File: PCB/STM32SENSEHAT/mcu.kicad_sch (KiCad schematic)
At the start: 26 parts, among them J1 USB_B_Micro, J2 Conn_01x24_Socket, J3 Conn_01x24_Socket, J5 Conn_01x24_Pin, J6 Conn_01x10_Pin, J7 Conn_01x04_Socket, J7 Conn_01x05_Pin, J8 Conn_01x24_Pin, J9 Conn_01x05_Socket, SW1 SW_Push, U3 FT230XQ, U6 CAT24C256

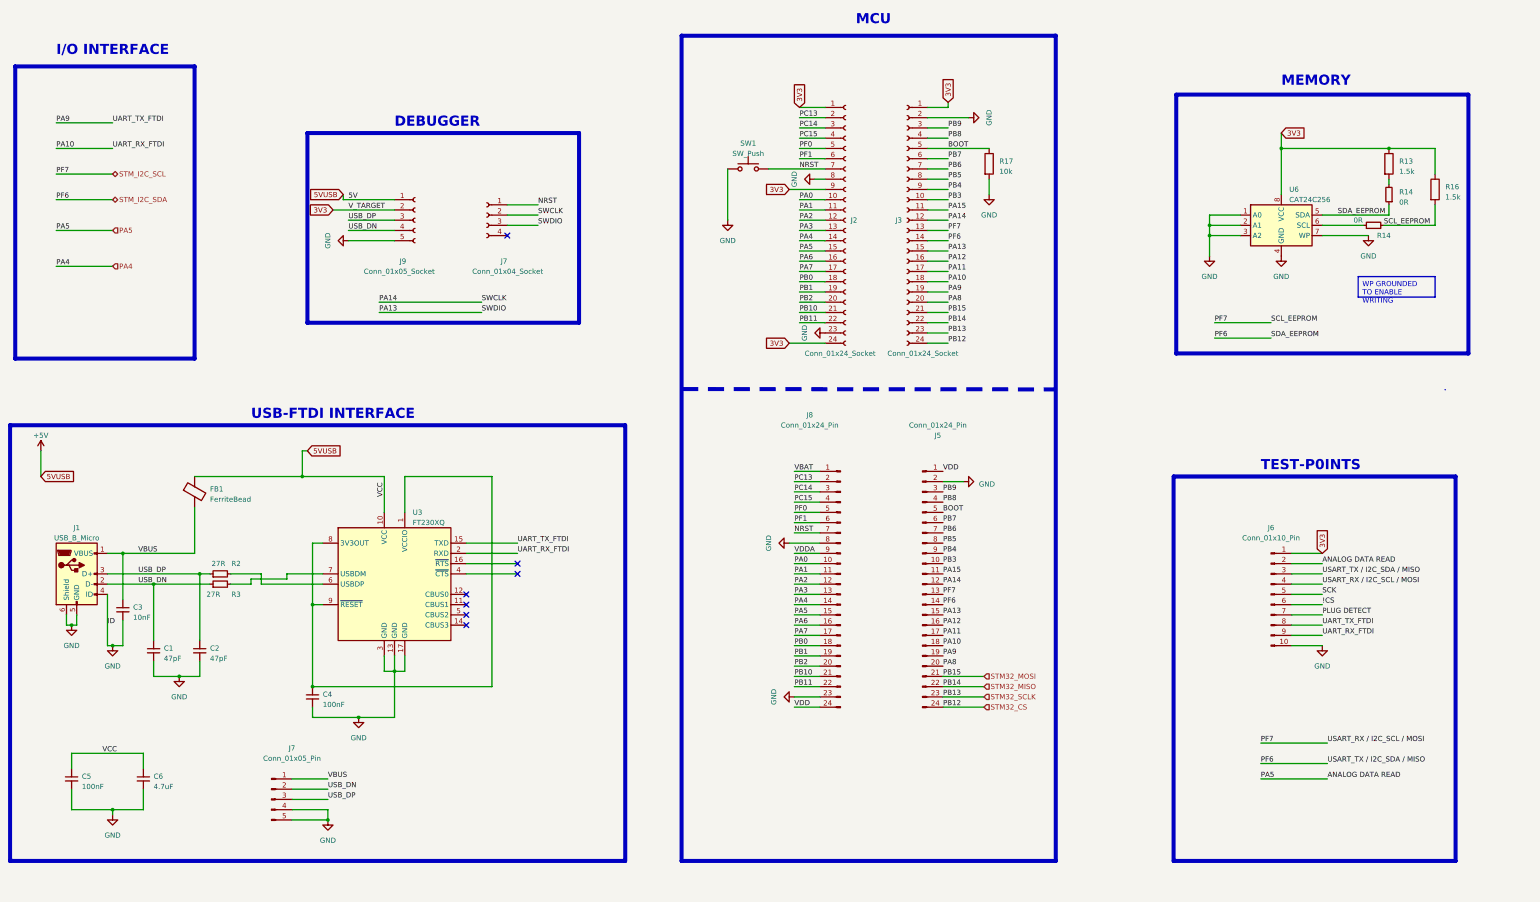
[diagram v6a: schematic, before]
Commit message: Rework of Power,MCU and Sensor Schematic
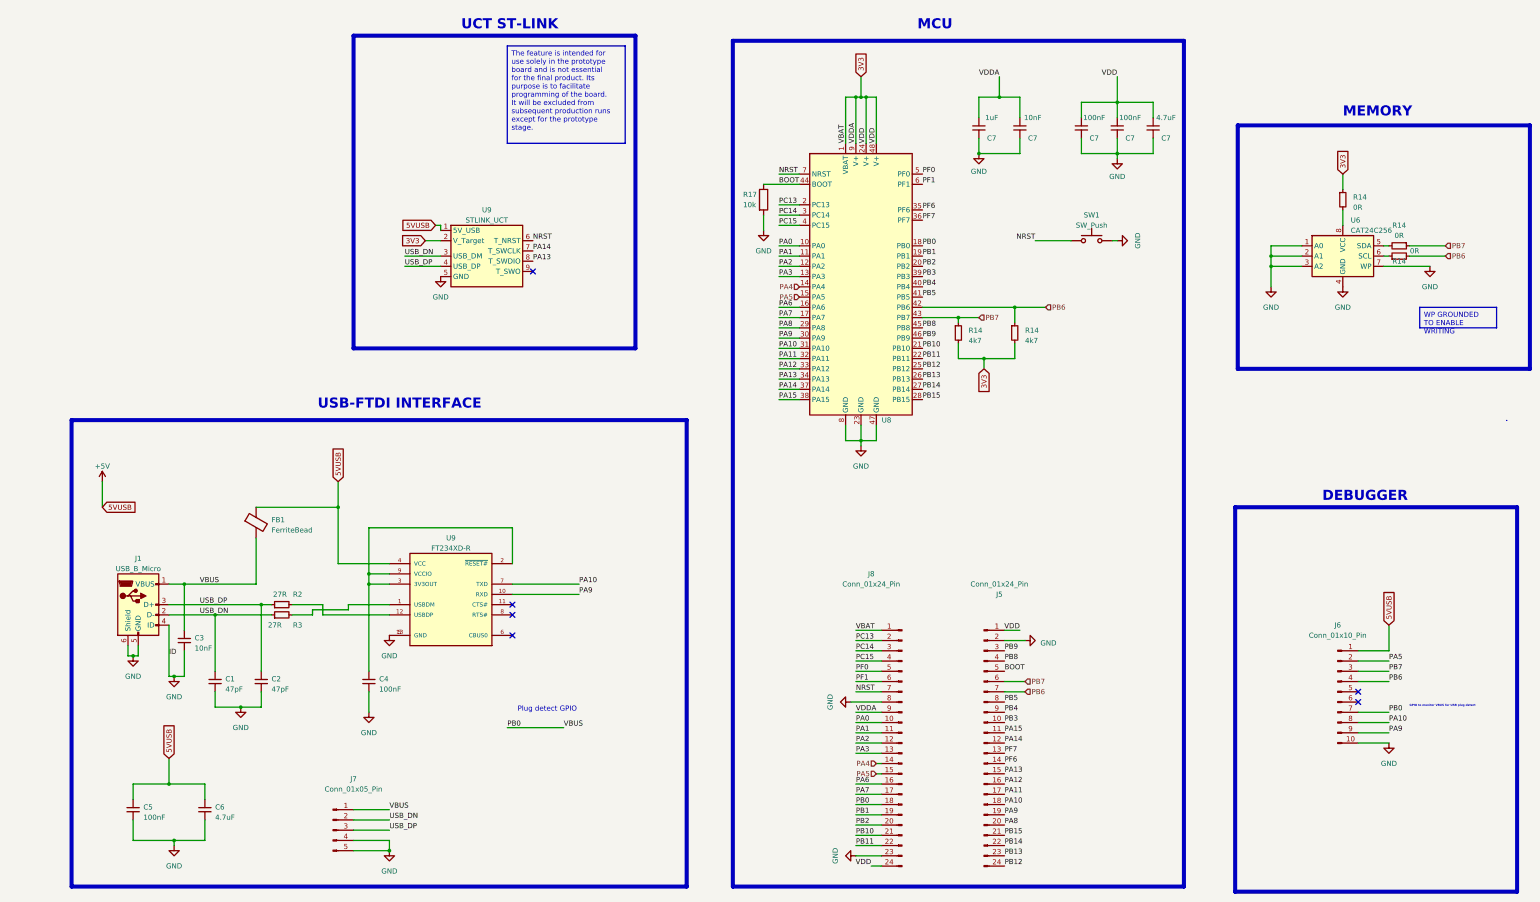
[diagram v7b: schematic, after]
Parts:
- removed J2, J3: Conn_01x24_Socket, Connector_PinSocket_2.54mm:PinSocket_1x24_P2.54mm_Vertical, symbol Connector:Conn_01x24_Socket
- removed J7: Conn_01x04_Socket, Connector_PinSocket_2.54mm:PinSocket_1x04_P2.54mm_Vertical, symbol Connector:Conn_01x04_Socket
- removed J9: Conn_01x05_Socket, Connector_PinSocket_2.54mm:PinSocket_1x05_P2.54mm_Vertical, symbol Connector:Conn_01x05_Socket
- removed R13, R16: 1.5k, Resistor_SMD:R_0805_2012Metric, symbol Device:R
- removed R14 (x2): 0R, Resistor_SMD:R_0805_2012Metric, symbol Device:R_Small
- removed U3: FT230XQ, Package_DFN_QFN:QFN-16-1EP_4x4mm_P0.65mm_EP2.1x2.1mm, symbol Interface_USB:FT230XQ
- added C7 (x2): 100nF, JLCfootprint:C0805, symbol Device:C_Small
- added C7: 1uF, JLCfootprint:C0805, symbol Device:C_Small
- added C7: 4.7uF, JLCfootprint:C0805, symbol Device:C_Small
- added C7: 10nF, JLCfootprint:C0805, symbol Device:C_Small
- added R14 (x2): 4k7, JLCfootprint:R0805, symbol Device:R_Small
- added R14 (x3): 0R, JLCfootprint:R0805, symbol Device:R_Small
- added U8: ~, footprints:STM32F051C6T6, symbol UCT:STM32F051C6TG6_Target
- added U9: FT234XD-R, JLCfootprint:DFN-12_L3.0-W3.0-P0.45-BL-EP, symbol FT234XD-R:FT234XD-R
- added U9: STLINK_UCT, footprints:STLINK_UCT, symbol UCT:STLINK_UCT
- C1, C2, C3, C4, C5, C6: footprint Capacitor_SMD:C_0805_2012Metric -> JLCfootprint:C0805
- FB1: footprint Resistor_SMD:R_0603_1608Metric -> JLCfootprint:L0603
- J1: footprint Connector_USB:USB_Micro-AB_Molex_47590-0001 -> footprints:USB_Conn_JLC_LCSC_C404969
- R17: footprint Resistor_SMD:R_0805_2012Metric -> JLCfootprint:R0805
- R2, R3: footprint Resistor_SMD:R_0603_1608Metric -> JLCfootprint:R0603
- U6: footprint Package_SO:SOIC-8-1EP_3.9x4.9mm_P1.27mm_EP2.41x3.3mm -> JLCfootprint:SOIC-8_L4.9-W3.9-P1.27-LS6.0-BL
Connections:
- net PLUG DETECT is gone; now on net PB0: J6.7 (Pin_7)
- net VBAT is gone; now on net 3V3: J8.1 (Pin_1)
- net VBUS is gone; now on net PB0: C3.1, FB1.2, J1.1 (VBUS), J7.1 (Pin_1)
- net VDD is gone; now on net 3V3: J5.1 (Pin_1), J8.24 (Pin_24)
- net VDDA is gone; now on net 3V3: J8.9 (Pin_9)
- net +5V: now also J6.1 (Pin_1), U9.1 (5V_USB), U9.4 (VCC)
- net 3V3: now also C7.1, C7.1, C7.1, C7.1, C7.1, R14.1, R14.2, R14.2, U8.1 (VBAT), U8.24 (V+), U8.48 (V+), U8.9 (V+), U9.2 (V_Target); no longer J6.1 (Pin_1), U6.8 (VCC)
- net BOOT: now also U8.44 (BOOT)
- net GND: now also C7.2, C7.2, C7.2, C7.2, C7.2, U8.23 (GND), U8.47 (GND), U8.8 (GND), U9.13 (GND), U9.5 (GND), U9.5 (GND)
- net NRST: now also U8.7 (NRST), U9.6 (T_NRST)
- net PA0: now also U8.10 (PA0)
- net PA1: now also U8.11 (PA1)
- net PA10: now also J6.8 (Pin_8), U8.31 (PA10), U9.7 (TXD); no longer J6.9 (Pin_9)
- net PA11: now also U8.32 (PA11)
- net PA12: now also U8.33 (PA12)
- net PA13: now also U8.34 (PA13), U9.8 (T_SWDIO)
- net PA14: now also U8.37 (PA14), U9.7 (T_SWCLK)
- net PA15: now also U8.38 (PA15)
- net PA2: now also U8.12 (PA2)
- net PA3: now also U8.13 (PA3)
- net PA4: now also U8.14 (PA4)
- net PA5: now also U8.15 (PA5)
- net PA6: now also U8.16 (PA6)
- net PA7: now also U8.17 (PA7)
- net PA8: now also U8.29 (PA8)
- net PA9: now also J6.9 (Pin_9), U8.30 (PA9), U9.10 (RXD); no longer J6.8 (Pin_8)
- net PB0: now also U8.18 (PB0)
- net PB1: now also U8.19 (PB1)
- net PB10: now also U8.21 (PB10)
- net PB11: now also U8.22 (PB11)
- net PB2: now also U8.20 (PB2)
- net PB3: now also U8.39 (PB3)
- net PB4: now also U8.40 (PB4)
- net PB5: now also U8.41 (PB5)
- net PB6: now also J6.4 (Pin_4), R14.1, R14.2, U8.42 (PB6)
- net PB7: now also J6.3 (Pin_3), R14.1, R14.1, U8.43 (PB7)
- net PB8: now also U8.45 (PB8)
- net PB9: now also U8.46 (PB9)
- net PC13: now also U8.2 (PC13)
- net PC14: now also U8.3 (PC14)
- net PC15: now also U8.4 (PC15)
- net PF0: now also U8.5 (PF0)
- net PF1: now also U8.6 (PF1)
- net USB_DN: now also U9.3 (USB_DM)
- net USB_DP: now also U9.4 (USB_DP)
- net at C4.1: now also U9.2 (~{RESET#}), U9.3 (3V3OUT), U9.9 (VCCIO)
- net at R3.2: now also U9.1 (USBDM)
- net at U6.6 (SCL): now also R14.1
- net at R2.2: now also U9.12 (USBDP)
- net !CS: no longer names the net of J6.6 (Pin_6)
- net SCK: no longer names the net of J6.5 (Pin_5)
- net STM32_CS renamed PB12
- net PB12: now also U8.25 (PB12)
- net STM32_MISO renamed PB14
- net PB14: now also U8.27 (PB14)
- net STM32_MOSI renamed PB15
- net PB15: now also U8.28 (PB15)
- net STM32_SCLK renamed PB13
- net PB13: now also U8.26 (PB13)
- net STM_I2C_SCL renamed PF7
- net PF7: now also U8.36 (PF7); no longer J6.4 (Pin_4)
- removed net STM_I2C_SDA: J5.14 (Pin_14), J6.3 (Pin_3), U6.5 (SDA)
- new net: R14.2, U6.5 (SDA)
- new net: R14.2, U6.8 (VCC)
- new net PF6: J5.14 (Pin_14), U8.35 (PF6)
- no-connect marks 7 -> 6
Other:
- note added: "GPIO to monitor VBUS for USB plug detect"
- note added: "Plug detect GPIO"
- note added: "UCT ST-LINK"
- note removed: "I/O INTERFACE"
- note removed: "TEST-P0INTS"

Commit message: PCB draft
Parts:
- C1, C2, C3, C4, C5, C6: footprint JLCfootprint:C0805 -> Capacitor_SMD:C_0805_2012Metric
- C7: footprint JLCfootprint:C0805 -> Capacitor_THT:C_Disc_D5.0mm_W2.5mm_P5.00mm
- R14, R17: footprint JLCfootprint:R0805 -> Resistor_SMD:R_0805_2012Metric
- R2, R3: footprint JLCfootprint:R0603 -> Resistor_SMD:R_0805_2012Metric
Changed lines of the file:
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@@
       (effects (font (size 1.27 1.27)) (justify left))
     )
-    (property "Footprint" "JLCfootprint:R0805" (at 252.73 92.71 0)
+    (property "Footprint" "Resistor_SMD:R_0805_2012Metric" (at 252.73 92.71 0)
       (effects (font (size 1.27 1.27)) hide)
     )
@@
       (effects (font (size 1.27 1.27)) (justify left))
     )
-    (property "Footprint" "JLCfootprint:R0603" (at 85.09 160.02 0)
+    (property "Footprint" "Resistor_SMD:R_0805_2012Metric" (at 85.09 160.02 0)
       (effects (font (size 1.27 1.27)) hide)
     )
@@
       (effects (font (size 1.27 1.27)) (justify left))
     )
-    (property "Footprint" "JLCfootprint:C0805" (at 60.96 168.91 0)
+    (property "Footprint" "Capacitor_SMD:C_0805_2012Metric" (at 60.96 168.91 0)
       (effects (font (size 1.27 1.27)) hide)
     )
@@
       (effects (font (size 1.27 1.27)) (justify left))
     )
-    (property "Footprint" "JLCfootprint:R0805" (at 266.7 92.71 0)
+    (property "Footprint" "Resistor_SMD:R_0805_2012Metric" (at 266.7 92.71 0)
       (effects (font (size 1.27 1.27)) hide)
     )
@@
       (effects (font (size 1.27 1.27)))
     )
-    (property "Footprint" "JLCfootprint:R0805" (at 361.95 71.12 0)
+    (property "Footprint" "Resistor_SMD:R_0805_2012Metric" (at 361.95 71.12 0)
       (effects (font (size 1.27 1.27)) hide)
     )
@@
       (effects (font (size 1.27 1.27)))
     )
-    (property "Footprint" "JLCfootprint:C0805" (at 283.21 41.91 0)
+    (property "Footprint" "Capacitor_THT:C_Disc_D5.0mm_W2.5mm_P5.00mm" (at 283.21 41.91 0)
       (effects (font (size 1.27 1.27)) hide)
     )
@@
       (effects (font (size 1.27 1.27)) (justify left))
     )
-    (property "Footprint" "JLCfootprint:R0603" (at 85.09 162.56 0)
+    (property "Footprint" "Resistor_SMD:R_0805_2012Metric" (at 85.09 162.56 0)
       (effects (font (size 1.27 1.27)) hide)
     )
@@
       (effects (font (size 1.27 1.27)))
     )
-    (property "Footprint" "JLCfootprint:C0805" (at 257.81 41.91 0)
+    (property "Footprint" "Capacitor_THT:C_Disc_D5.0mm_W2.5mm_P5.00mm" (at 257.81 41.91 0)
       (effects (font (size 1.27 1.27)) hide)
     )
@@
       (effects (font (size 1.27 1.27)) (justify left))
     )
-    (property "Footprint" "JLCfootprint:C0805" (at 66.04 210.82 0)
+    (property "Footprint" "Capacitor_SMD:C_0805_2012Metric" (at 66.04 210.82 0)
       (effects (font (size 1.27 1.27)) hide)
     )
@@
       (effects (font (size 1.27 1.27)) (justify left))
     )
-    (property "Footprint" "JLCfootprint:C0805" (at 68.58 179.07 0)
+    (property "Footprint" "Capacitor_SMD:C_0805_2012Metric" (at 68.58 179.07 0)
       (effects (font (size 1.27 1.27)) hide)
     )
@@
       (effects (font (size 1.27 1.27)) (justify left))
     )
-    (property "Footprint" "JLCfootprint:C0805" (at 106.68 179.07 0)
+    (property "Footprint" "Capacitor_SMD:C_0805_2012Metric" (at 106.68 179.07 0)
       (effects (font (size 1.27 1.27)) hide)
     )
@@
       (effects (font (size 1.27 1.27)) (justify left))
     )
-    (property "Footprint" "JLCfootprint:C0805" (at 80.01 179.07 0)
+    (property "Footprint" "Capacitor_SMD:C_0805_2012Metric" (at 80.01 179.07 0)
       (effects (font (size 1.27 1.27)) hide)
     )
@@
       (effects (font (size 1.27 1.27)) (justify left))
     )
-    (property "Footprint" "JLCfootprint:C0805" (at 48.26 210.82 0)
+    (property "Footprint" "Capacitor_SMD:C_0805_2012Metric" (at 48.26 210.82 0)
       (effects (font (size 1.27 1.27)) hide)
     )
@@
       (effects (font (size 1.27 1.27)) (justify left))
     )
-    (property "Footprint" "JLCfootprint:R0805" (at 347.98 59.69 0)
+    (property "Footprint" "Resistor_SMD:R_0805_2012Metric" (at 347.98 59.69 0)
       (effects (font (size 1.27 1.27)) hide)
     )
@@
       (effects (font (size 1.27 1.27)) (justify left))
     )
-    (property "Footprint" "JLCfootprint:R0805" (at 202.692 59.69 90)
+    (property "Footprint" "Resistor_SMD:R_0805_2012Metric" (at 202.692 59.69 90)
       (effects (font (size 1.27 1.27)) hide)
     )
@@
       (effects (font (size 1.27 1.27)))
     )
-    (property "Footprint" "JLCfootprint:R0805" (at 361.95 73.66 0)
+    (property "Footprint" "Resistor_SMD:R_0805_2012Metric" (at 361.95 73.66 0)
       (effects (font (size 1.27 1.27)) hide)
     )
@@
       (effects (font (size 1.27 1.27)))
     )
-    (property "Footprint" "JLCfootprint:C0805" (at 300.99 41.91 0)
+    (property "Footprint" "Capacitor_THT:C_Disc_D5.0mm_W2.5mm_P5.00mm" (at 300.99 41.91 0)
       (effects (font (size 1.27 1.27)) hide)
     )
@@
       (effects (font (size 1.27 1.27)))
     )
-    (property "Footprint" "JLCfootprint:C0805" (at 267.97 41.91 0)
+    (property "Footprint" "Capacitor_THT:C_Disc_D5.0mm_W2.5mm_P5.00mm" (at 267.97 41.91 0)
       (effects (font (size 1.27 1.27)) hide)
     )
@@
       (effects (font (size 1.27 1.27)))
     )
-    (property "Footprint" "JLCfootprint:C0805" (at 292.1 41.91 0)
-      (effects (font (size 1.27 1.27)) hide)
-    )
+    (property "Footprint" "Capacitor_THT:C_Disc_D5.0mm_W2.5mm_P5.00mm" (at 292.1 41.91 0)
+      (effects (font (size 1.27 1.27)) hide)
+    )
